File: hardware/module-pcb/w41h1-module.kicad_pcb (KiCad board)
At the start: 2 copper layers, 40 x 20.5 mm, 31 parts, among them J1 A/C port (2.0 mm, verify), J2 PROG (not fitted), U1 ESP32-C3-WROOM-02, U2 TLV62569DBV, U3 SP3485EN

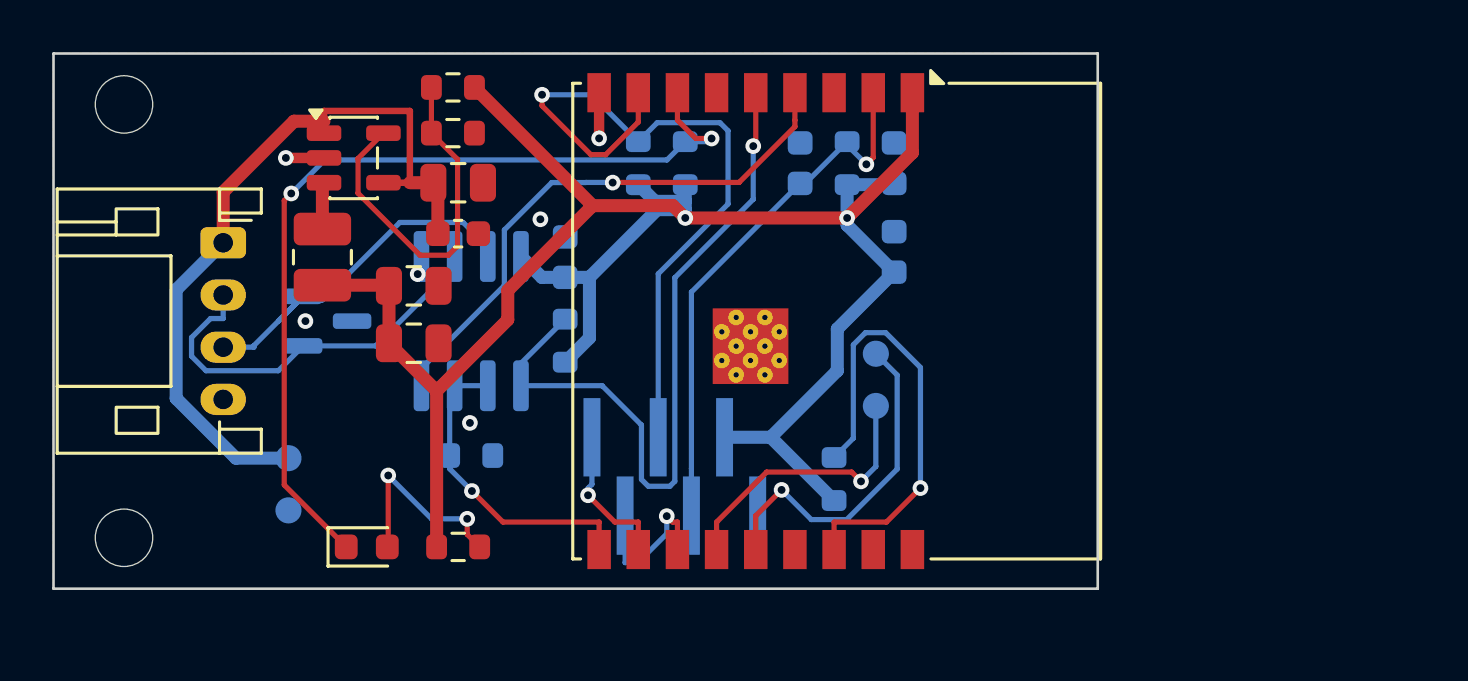
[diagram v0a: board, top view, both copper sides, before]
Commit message: hardware: review fixes for the module PCB, part numbers, fab export
Checked every IC against its datasheet (TLV62569, ESP32-C3-WROOM-02, SP3485):
pinouts, the 0.6 V feedback reference, strapping resistors and the EN delay
match. Two changes came out of it:

- The regulator's output capacitance was above the 47 uF the datasheet allows:
  C3 is 10 uF now.
- The autorouter gave the feedback node a long detour. The regulator is placed
  and pre-routed by hand now: input capacitor, inductor and output capacitor
  next to the part, short switch and feedback nodes.

Also: MPN and LCSC fields on every fitted part, stitch.py keeps vias out of
pads, scripts/fab.sh writes gerbers, drill, BOM, placement file, schematic PDF
and STEP into fab/ after a clean ERC and DRC.

Assisted-by: AI
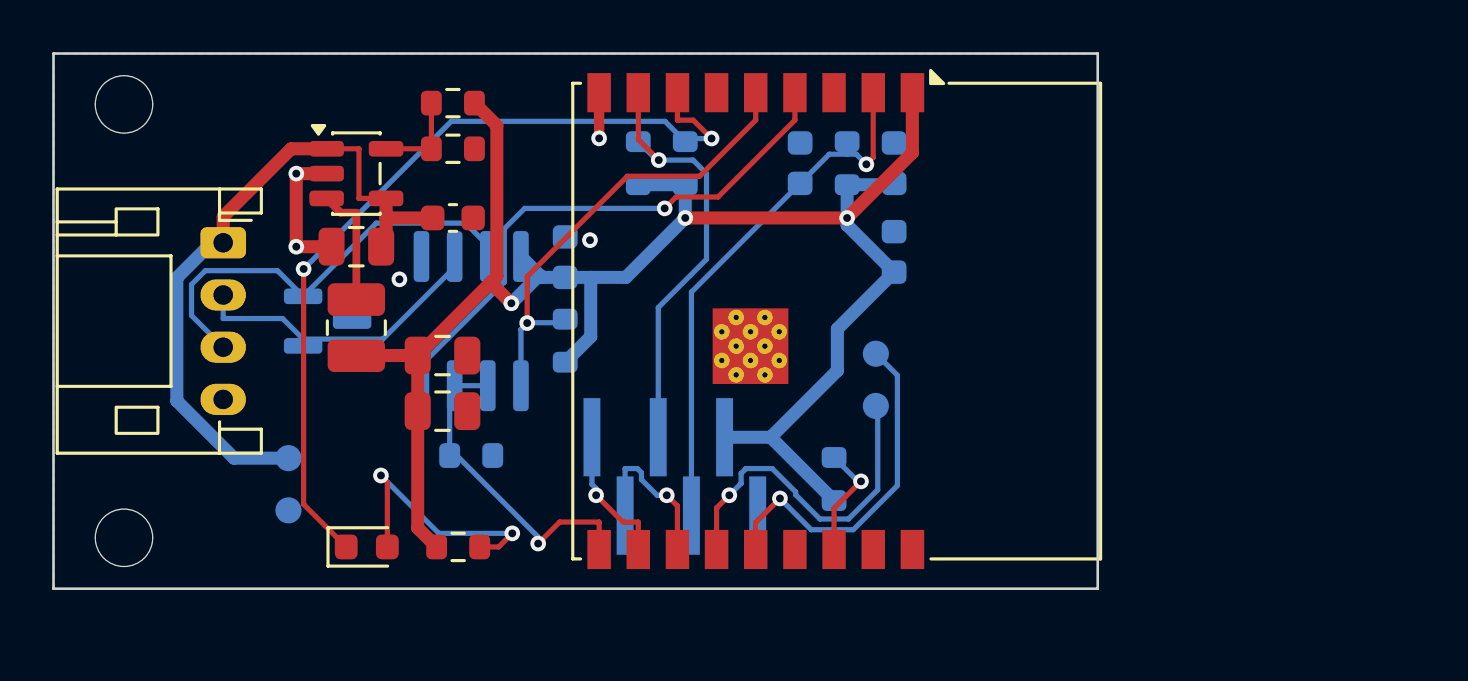
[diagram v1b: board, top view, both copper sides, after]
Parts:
- C3: value 22u 6.3V -> 10u
- D1: value status -> red
- moved C1 4.61 mm to (111.6, 107.4), turned to 180 degrees
- moved L1 3.00 mm to (111.6, 110.5)
- moved C2 2.89 mm to (114.9, 111.6)
- moved C3 2.82 mm to (114.9, 113.7)
- moved C8 0.63 mm to (115.3, 106.3)
- moved U2 0.61 mm to (111.6, 104.6)
- moved R1 0.60 mm to (115.3, 101.9)
- moved R2 0.60 mm to (115.3, 103.7)
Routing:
- net /IO2: track 17.5 -> 4.45 mm
- net /IO9: track 27.7 -> 16.9 mm
- net /FB: track 14.1 -> 3.49 mm
- net /RS485_RX: track 28.2 -> 18.1 mm
- net /+3V3: track 79.1 -> 69.7 mm, vias 2 -> 3
- net /GND: track 3.21 -> 7.06 mm, vias 6 -> 5
- net /RS485_A: track 15.5 -> 11.9 mm
- net /+5V: track 29.7 -> 26.2 mm
- net /SW: track 1.80 -> 4.70 mm
- net /RS485_B: track 14.2 -> 16.8 mm
- net /USB_D-: track 10.6 -> 13.2 mm
- net /LED_A: track 7.74 -> 10.2 mm
- net /IO8: track 34.3 -> 32.3 mm
- net /RS485_DE: track 12.2 -> 12.7 mm

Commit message: hardware: case for the module PCB, silkscreen labels, final fab outputs
- hardware/module-case: a CadQuery script for a two-part case, 53 x 25 x 11.5 mm.
  Two M2 screws pass through the lid and the board's mounting holes into the base.
  The script checks both parts against the board's STEP model: no overlap.
- Silkscreen labels for the A/C connector pins, the programming pads and the test pads.
- J2 (bare programming pads) is marked as not fitted, so it stays out of the BOM,
  the placement file and the 3D model.
- fab.sh sets the export origin to the board corner and drops unsourced BOM rows.
- READMEs for both, with what was checked and what is still an estimate.

Assisted-by: AI
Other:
- board text added: "1"
- board text added: "1 GND 2 3V3"
- board text added: "3 EN 4 IO9"
- board text added: "5 TX 6 RX"
- board text added: "5V"
- board text added: "A"
- board text added: "B"
- board text added: "D+"
- board text added: "D-"
- board text added: "G"
- board text added: "GND"
- board text added: "PROG"
- board text added: "W41H1-C3 rev A"
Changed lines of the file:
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@@
 			)
 		)
-		(attr smd)
+		(attr smd exclude_from_pos_files dnp)
 		(duplicate_pad_numbers_are_jumpers no)
 		(fp_line
@@
 		(layer "Edge.Cuts")
 	)
+	(gr_text "A"
+		(at 108.7 109.25 0)
+		(layer "F.SilkS")
+		(effects
+			(font
+				(size 0.8 0.8)
+				(thickness 0.15)
+			)
+		)
+	)
+	(gr_text "B"
+		(at 108.7 111.25 0)
+		(layer "F.SilkS")
+		(effects
+			(font
+				(size 0.8 0.8)
+				(thickness 0.15)
+			)
+		)
+	)
+	(gr_text "G"
+		(at 108.7 113.25 0)
+		(layer "F.SilkS")
+		(effects
+			(font
+				(size 0.8 0.8)
+				(thickness 0.15)
+			)
+		)
+	)
+	(gr_text "5V"
+		(at 108.9 107.25 0)
+		(layer "F.SilkS")
+		(effects
+			(font
+				(size 0.8 0.8)
+				(thickness 0.15)
+			)
+		)
+	)
+	(gr_text "W41H1-C3 rev A"
+		(at 114 116.2 0)
+		(layer "F.SilkS")
+		(effects
+			(font
+				(size 0.8 0.8)
+				(thickness 0.15)
+			)
+		)
+	)
+	(gr_text "GND"
+		(at 106.9 117.5 0)
+		(layer "B.SilkS")
+		(effects
+			(font
+				(size 0.8 0.8)
+				(thickness 0.15)
+			)
+			(justify mirror)
+		)
+	)
+	(gr_text "5V"
+		(at 107.3 115.5 0)
+		(layer "B.SilkS")
+		(effects
+			(font
+				(size 0.8 0.8)
+				(thickness 0.15)
+			)
+			(justify mirror)
+		)
+	)
+	(gr_text "PROG"
+		(at 114.8 116.9 0)
+		(layer "B.SilkS")
+		(effects
+			(font
+				(size 0.8 0.8)
+				(thickness 0.15)
+			)
+			(justify mirror)
+		)
+	)
+	(gr_text "1 GND 2 3V3"
+		(at 114.8 117.95 0)
+		(layer "B.SilkS")
+		(effects
+			(font
+				(size 0.8 0.8)
+				(thickness 0.15)
+			)
+			(justify mirror)
+		)
+	)
+	(gr_text "3 EN 4 IO9"
+		(at 114.8 119 0)
+		(layer "B.SilkS")
+		(effects
+			(font
+				(size 0.8 0.8)
+				(thickness 0.15)
+			)
+			(justify mirror)
+		)
+	)
+	(gr_text "5 TX 6 RX"
+		(at 114.8 120.05 0)
+		(layer "B.SilkS")
+		(effects
+			(font
+				(size 0.8 0.8)
+				(thickness 0.15)
+			)
+			(justify mirror)
+		)
+	)
+	(gr_text "1"
+		(at 128.199999 118.9 0)
+		(layer "B.SilkS")
+		(effects
+			(font
+				(size 0.8 0.8)
+				(thickness 0.15)
+			)
+			(justify mirror)
+		)
+	)
+	(gr_text "D+"
+		(at 133.199999 111.5 0)
+		(layer "B.SilkS")
+		(effects
+			(font
+				(size 0.8 0.8)
+				(thickness 0.15)
+			)
+			(justify mirror)
+		)
+	)
+	(gr_text "D-"
+		(at 133.199999 113.5 0)
+		(layer "B.SilkS")
+		(effects
+			(font
+				(size 0.8 0.8)
+				(thickness 0.15)
+			)
+			(justify mirror)
+		)
+	)
 	(segment
 		(start 112.74 103.65)
@@
 	)
 	(zone
-		(net "/GND")
-		(layer "F.Cu")
-		(name "GND")
-		(hatch edge 0.5)
-		(connect_pads yes
-			(clearance 0.25)
-		)
-		(min_thickness 0.2)
-		(fill yes
-			(thermal_gap 0.5)
-			(thermal_bridge_width 0.5)
-			(island_removal_mode 0)
-		)
-		(polygon
-			(pts
-				(xy 100 100) (xy 140 100) (xy 140 120.5) (xy 100 120.5)
-			)
-		)
-	)
-	(zone
 		(layer "F.Cu")
 		(name "under-module")
@@
 	)
 	(zone
+		(net "/GND")
+		(layer "F.Cu")
+		(name "GND")
+		(hatch edge 0.5)
+		(connect_pads yes
+			(clearance 0.25)
+		)
+		(min_thickness 0.2)
+		(fill yes
+			(thermal_gap 0.5)
+			(thermal_bridge_width 0.5)
+			(island_removal_mode 0)
+		)
+		(polygon
+			(pts
+				(xy 100 100) (xy 140 100) (xy 140 120.5) (xy 100 120.5)
+			)
+		)
+	)
+	(zone
 		(layers "F.Cu" "B.Cu")
 		(name "edge-bottom")
@@
 	(zone
 		(layers "F.Cu" "B.Cu")
-		(name "edge-left")
+		(name "edge-top")
 		(hatch edge 0.5)
 		(connect_pads
@@
 		(polygon
 			(pts
-				(xy 100 100) (xy 100.6 100) (xy 100.6 120.5) (xy 100 120.5)
+				(xy 100 100) (xy 140 100) (xy 140 100.6) (xy 100 100.6)
 			)
 		)
@@
 	(zone
 		(layers "F.Cu" "B.Cu")
-		(name "edge-top")
+		(name "edge-left")
 		(hatch edge 0.5)
 		(connect_pads
@@
 		(polygon
 			(pts
-				(xy 100 100) (xy 140 100) (xy 140 100.6) (xy 100 100.6)
+				(xy 100 100) (xy 100.6 100) (xy 100.6 120.5) (xy 100 120.5)
 			)
 		)

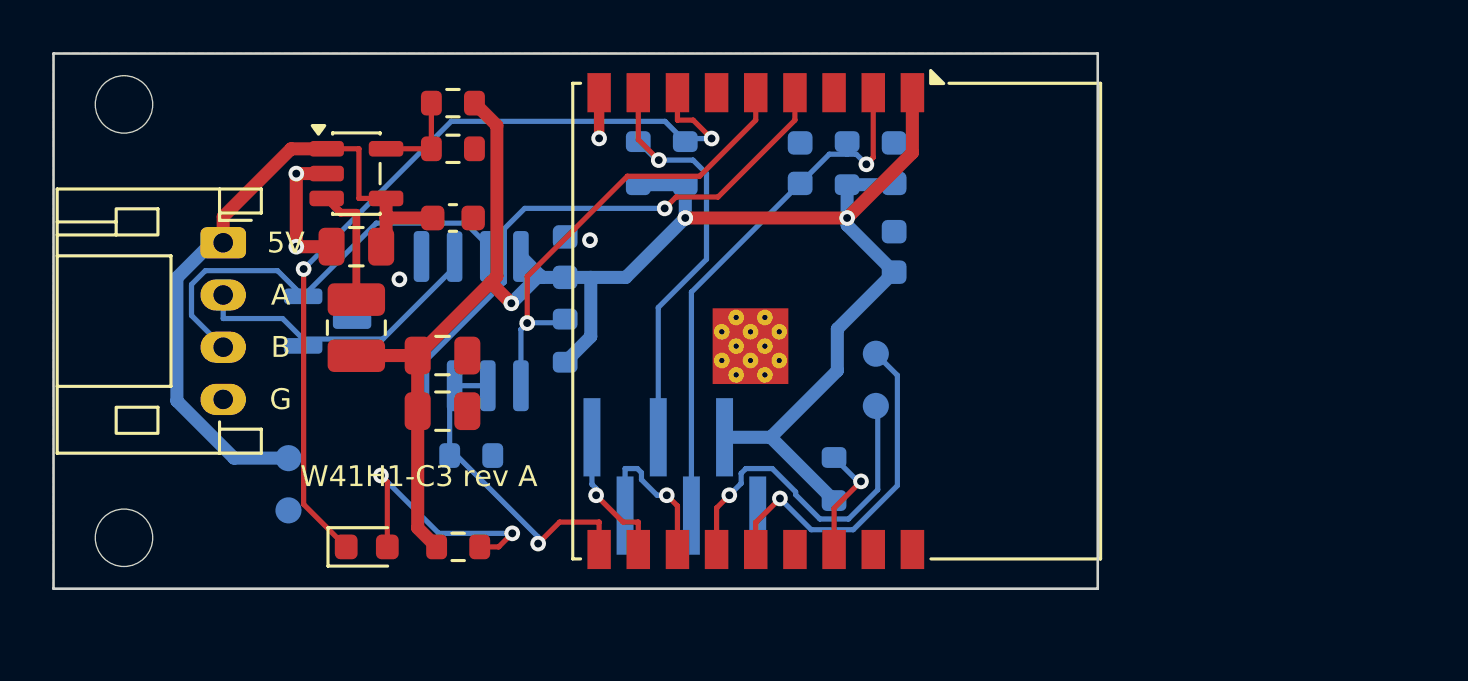
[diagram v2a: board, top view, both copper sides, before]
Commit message: hardware: rev B, one-sided assembly and standard drills to cut the JLCPCB price
The quote for rev A showed where the money went: the module footprint's 0.2 mm
thermal vias brought three surcharges (small holes, via covering, Kelvin test),
and parts on both sides forced Standard assembly with edge rails.

- Every assembled part is on the top side now, so Economic assembly applies.
  Only bare pads (programming, test points) stay on the bottom.
- Four of the module's thermal vias become 0.3 mm and the rest plain copper:
  the board's minimum drill is the standard 0.3 mm again.
- The board is 52 x 22 mm, no longer the stock module's size; the case follows
  the board (65 x 26.2 x 11.5 mm) and still has no overlap with it.
- fab.sh lists every BOM reference: JLCPCB rejected ranges like R3-R5.

Assisted-by: AI
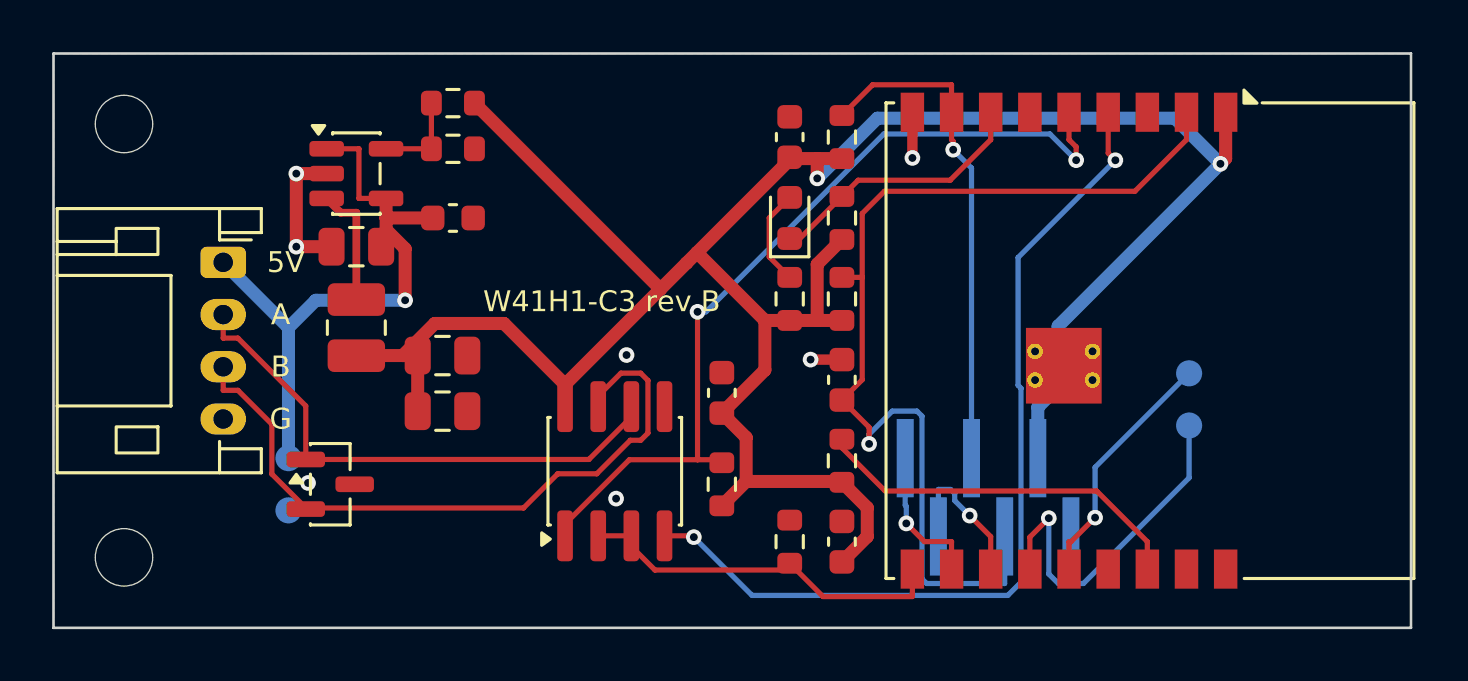
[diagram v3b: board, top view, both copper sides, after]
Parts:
- C4, C5, C6, C7, D2, R3, R4, R5, R7, R8, R9, U3: moved to F.Cu
- moved D1 20.5 mm to (128.2, 106.3), turned to 90 degrees
- moved R6 15.9 mm to (128.2, 109.4), turned to 90 degrees
- moved R8 12.6 mm to (128.2, 118.7), turned to 90 degrees
- moved J2 12.0 mm to (135.8, 117.0)
- moved TP1 12.0 mm to (143.5, 114.2)
- moved TP2 12.0 mm to (143.5, 112.2)
- moved U1 12.0 mm to (138.9, 111.0)
- moved C5 11.3 mm to (130.2, 118.7)
- moved C6 8.45 mm to (130.2, 112.5)
- moved R9 8.14 mm to (125.6, 116.5)
- moved U3 7.96 mm to (121.5, 116.0)
- moved C7 7.94 mm to (125.6, 113.0)
- moved R4 7.86 mm to (130.2, 103.2)
- moved R5 6.36 mm to (130.2, 106.3)
- moved D2 6.25 mm to (110.6, 116.5)
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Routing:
- net /+3V3: track 69.7 -> 97.7 mm, vias 3 -> 2
- net /IO8: track 32.3 -> 10.3 mm, vias 2 -> 0
- net /EN: track 20.9 -> 39.1 mm
- net /RS485_RX: track 18.1 -> 32.9 mm, vias 1 -> 2
- net /RS485_TX: track 21.2 -> 34.5 mm, vias 1 -> 2
- net /IO2: track 4.45 -> 14.6 mm, vias 1 -> 0
- net /RS485_B: track 16.8 -> 26.2 mm
- net /RS485_A: track 11.9 -> 20.7 mm
- net /LED_A: track 10.2 -> 3.71 mm, vias 2 -> 0
- net /USB_D+: track 13.4 -> 9.45 mm
- net /IO9: track 16.9 -> 19.3 mm
- net /+5V: track 26.2 -> 24.3 mm, vias 0 -> 1
- net /RS485_DE: track 12.7 -> 14.5 mm, vias 1 -> 0
- net /GND: track 7.06 -> 8.26 mm, vias 5 -> 7
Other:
- board size 40 x 20.5 mm -> 52 x 22 mm
- board text added: "W41H1-C3 rev B"
- board text removed: "W41H1-C3 rev A"

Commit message: hardware: give C1 and C2 the same value so they share one BOM line
Both are the same 22 uF part. Different value text made JLCPCB's importer warn
about two BOM lines matched to one part.

Assisted-by: AI
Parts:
- C1: value 22u 10V -> 22u
- C2: value 22u 6.3V -> 22u
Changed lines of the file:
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@@
 			)
 		)
-		(property "Value" "22u 6.3V"
+		(property "Value" "22u"
 			(at 0 1.68 0)
 			(layer "F.Fab")
@@
 			)
 		)
-		(property "Value" "22u 10V"
+		(property "Value" "22u"
 			(at 0 1.68 180)
 			(layer "F.Fab")
